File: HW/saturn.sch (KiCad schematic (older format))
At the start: 0 parts

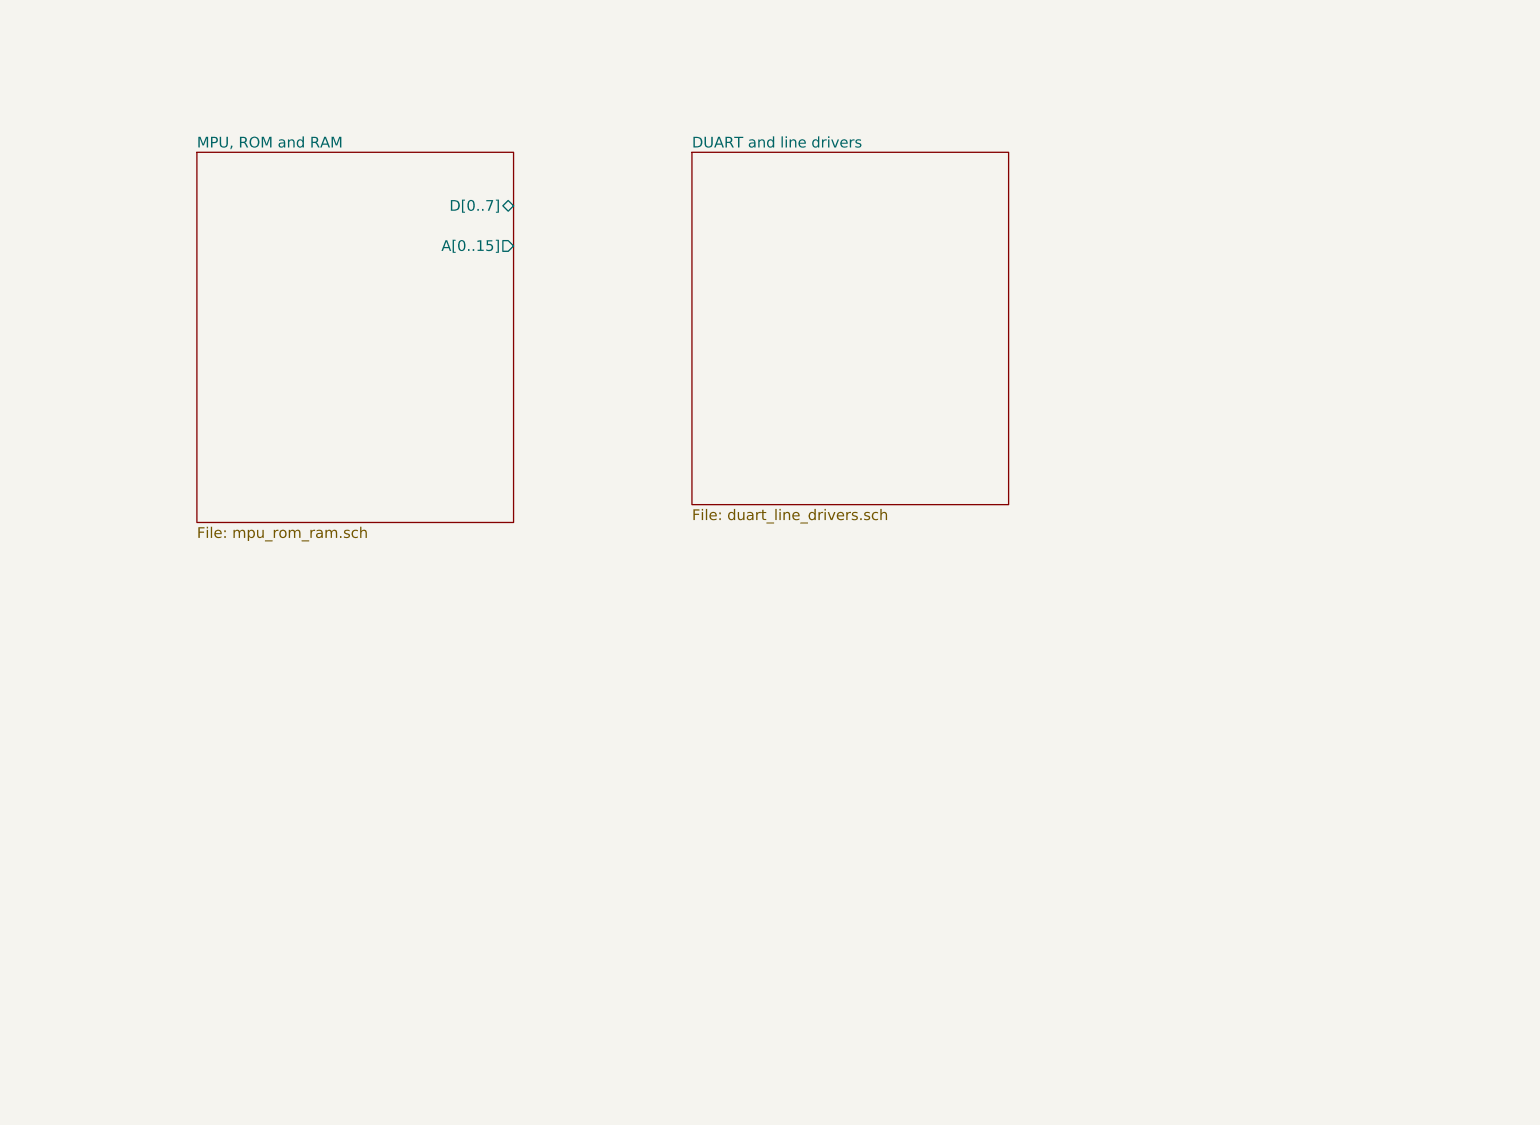
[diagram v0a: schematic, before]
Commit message: Added ram, vias, rtc and ide connector. Managed to delete Pluto's CPLD schemas.
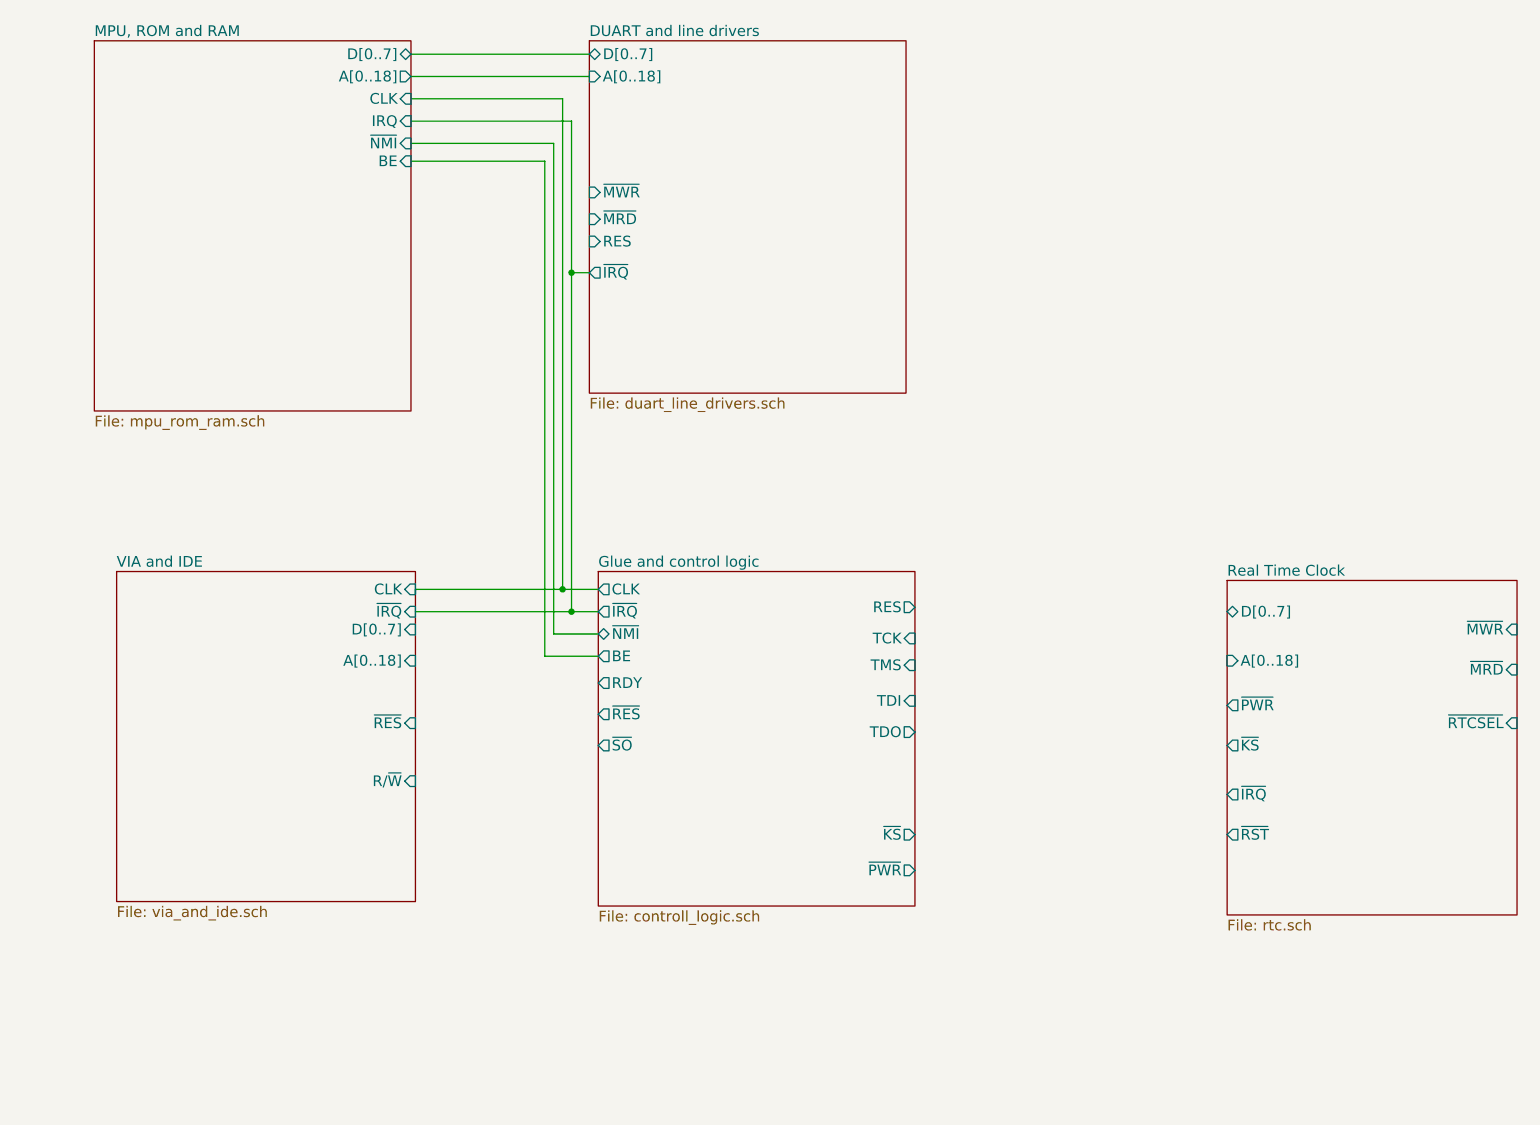
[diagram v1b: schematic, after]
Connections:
- wire segments 0 -> 16
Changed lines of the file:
@@
 EESchema Schematic File Version 2
+LIBS:saturn-rescue
 LIBS:power
 LIBS:device
@@
 LIBS:contrib
 LIBS:valves
+LIBS:saturn
+LIBS:65xx
 LIBS:pluto
-LIBS:65xx
+LIBS:Oscillators
+LIBS:switches
 LIBS:saturn-cache
 EELAYER 25 0
@@
 $Descr A4 11693 8268
 encoding utf-8
-Sheet 1 3
+Sheet 1 6
 Title "Saturn SBC"
 Date "2017-06-28"
@@
 $EndDescr
 $Sheet
-S 1800 1625 1775 2075
+S 1225 1000 1775 2075
 U 5952FC78
 F0 "MPU, ROM and RAM" 60
 F1 "mpu_rom_ram.sch" 60
-F2 "D[0..7]" B R 3575 1925 60
-F3 "A[0..15]" O R 3575 2150 60
+F2 "D[0..7]" B R 3000 1075 60
+F3 "A[0..18]" O R 3000 1200 60
+F4 "CLK" I R 3000 1325 60
+F5 "IRQ" I R 3000 1450 60
+F6 "~NMI" I R 3000 1575 60
+F7 "BE" I R 3000 1675 60
 $EndSheet
 $Sheet
-S 4575 1625 1775 1975
+S 4000 1000 1775 1975
 U 5952FC81
 F0 "DUART and line drivers" 60
 F1 "duart_line_drivers.sch" 60
+F2 "D[0..7]" B L 4000 1075 60
+F3 "~MWR" I L 4000 1850 60
+F4 "~MRD" I L 4000 2000 60
+F5 "RES" I L 4000 2125 60
+F6 "~IRQ" O L 4000 2300 60
+F7 "A[0..18]" I L 4000 1200 60
+$EndSheet
+Wire Wire Line
+	3000 1075 4000 1075
+Wire Wire Line
+	3000 1200 4000 1200
+$Sheet
+S 1350 3975 1675 1850
+U 5A3B21BC
+F0 "VIA and IDE" 60
+F1 "via_and_ide.sch" 60
+F2 "D[0..7]" I R 3025 4300 60
+F3 "A[0..18]" I R 3025 4475 60
+F4 "CLK" I R 3025 4075 60
+F5 "~RES" I R 3025 4825 60
+F6 "~IRQ" I R 3025 4200 60
+F7 "R/~W" I R 3025 5150 60
+$EndSheet
+$Sheet
+S 4050 3975 1775 1875
+U 5A3B356D
+F0 "Glue and control logic" 60
+F1 "controll_logic.sch" 60
+F2 "CLK" O L 4050 4075 60
+F3 "~IRQ" O L 4050 4200 60
+F4 "~NMI" B L 4050 4325 60
+F5 "BE" O L 4050 4450 60
+F6 "RDY" O L 4050 4600 60
+F7 "~PWR" O R 5825 5650 60
+F8 "~RES" O L 4050 4775 60
+F9 "~SO" O L 4050 4950 60
+F10 "RES" O R 5825 4175 60
+F11 "TCK" I R 5825 4350 60
+F12 "TMS" I R 5825 4500 60
+F13 "TDI" I R 5825 4700 60
+F14 "TDO" O R 5825 4875 60
+F15 "~KS" O R 5825 5450 60
+$EndSheet
+Wire Wire Line
+	3000 1450 3900 1450
+Wire Wire Line
+	3900 1450 3900 4200
+Wire Wire Line
+	3900 2300 4000 2300
+Wire Wire Line
+	3025 4200 4050 4200
+Connection ~ 3900 2300
+Wire Wire Line
+	3000 1325 3850 1325
+Wire Wire Line
+	3850 1325 3850 4075
+Wire Wire Line
+	3025 4075 4050 4075
+Wire Wire Line
+	3000 1575 3800 1575
+Wire Wire Line
+	3800 1575 3800 4325
+Wire Wire Line
+	3800 4325 4050 4325
+Wire Wire Line
+	3000 1675 3750 1675
+Wire Wire Line
+	3750 1675 3750 4450
+Wire Wire Line
+	3750 4450 4050 4450
+Wire Wire Line
+	3025 4100 3025 4075
+Connection ~ 3850 4075
+Connection ~ 3900 4200
+$Sheet
+S 7575 4025 1625 1875
+U 5A3D7428
+F0 "Real Time Clock" 60
+F1 "rtc.sch" 60
+F2 "D[0..7]" B L 7575 4200 60
+F3 "A[0..18]" I L 7575 4475 60
+F4 "~PWR" O L 7575 4725 60
+F5 "~KS" O L 7575 4950 60
+F6 "~IRQ" O L 7575 5225 60
+F7 "~RST" O L 7575 5450 60
+F8 "~MWR" I R 9200 4300 60
+F9 "~MRD" I R 9200 4525 60
+F10 "~RTCSEL" I R 9200 4825 60
 $EndSheet
 $EndSCHEMATC

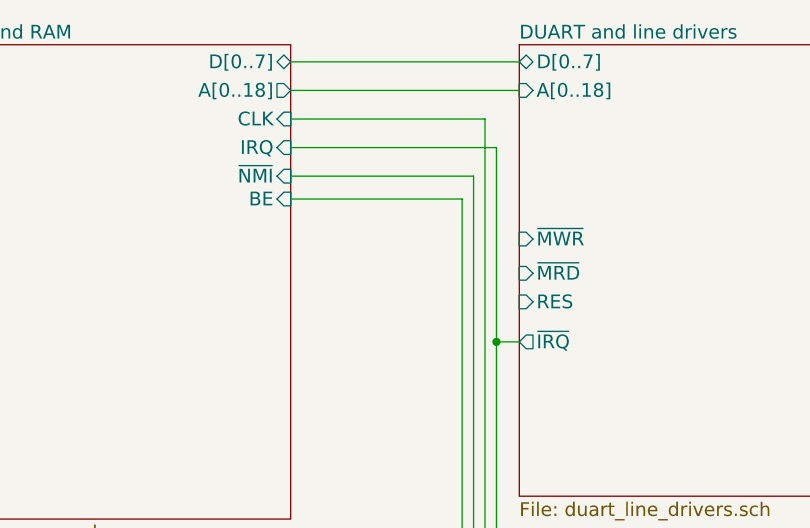
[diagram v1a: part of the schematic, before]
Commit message: Address, databus and control signals added to RAM and ROM
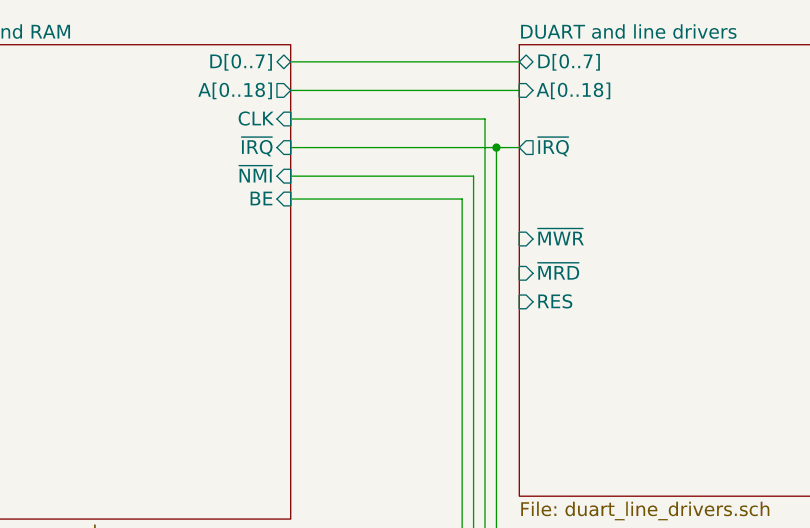
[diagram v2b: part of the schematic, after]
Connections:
- wire segments 16 -> 15
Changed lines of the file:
@@
 Sheet 1 6
 Title "Saturn SBC"
-Date "2017-06-28"
-Rev "1.0"
+Date "2017-12-23"
+Rev "0.1"
 Comp "Linux Grotto"
-Comment1 ""
-Comment2 ""
-Comment3 ""
-Comment4 ""
+Comment1 "Control logic is implemented using an ispMACH4A5"
+Comment2 "IDE interface realised with two VIA 65C22"
+Comment3 "Serial Communication with a 28L92 and MAX238"
+Comment4 "Real Time clock, a DS1511Y"
 $EndDescr
 $Sheet
@@
 F3 "A[0..18]" O R 3000 1200 60
 F4 "CLK" I R 3000 1325 60
-F5 "IRQ" I R 3000 1450 60
-F6 "~NMI" I R 3000 1575 60
-F7 "BE" I R 3000 1675 60
+F5 "~NMI" I R 3000 1575 60
+F6 "BE" I R 3000 1675 60
+F7 "~IRQ" I R 3000 1450 60
 $EndSheet
 $Sheet
@@
 F4 "~MRD" I L 4000 2000 60
 F5 "RES" I L 4000 2125 60
-F6 "~IRQ" O L 4000 2300 60
+F6 "~IRQ" O L 4000 1450 60
 F7 "A[0..18]" I L 4000 1200 60
 $EndSheet
@@
 $EndSheet
 Wire Wire Line
-	3000 1450 3900 1450
+	3000 1450 4000 1450
 Wire Wire Line
 	3900 1450 3900 4200
 Wire Wire Line
-	3900 2300 4000 2300
-Wire Wire Line
 	3025 4200 4050 4200
-Connection ~ 3900 2300
 Wire Wire Line
 	3000 1325 3850 1325
@@
 F10 "~RTCSEL" I R 9200 4825 60
 $EndSheet
+Connection ~ 3900 1450
 $EndSCHEMATC

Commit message: Finished RAM/ROM/CPU control signals.
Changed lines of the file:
@@
 F6 "BE" I R 3000 1675 60
 F7 "~IRQ" I R 3000 1450 60
+F8 "~MRD" I L 1225 2075 60
+F9 "~MWR" I L 1225 1675 60
+F10 "~RAM0" I L 1225 1800 60
+F11 "~RAM1" I L 1225 1925 60
+F12 "~ROM" I L 1225 2200 60
+F13 "R/~W" O L 1225 2325 60
+F14 "VDA" O L 1225 2425 60
+F15 "VPA" O L 1225 2550 60
+F16 "~RES" I L 1225 2700 60
+F17 "/ABT" I L 1225 1550 60
+F18 "RDY" I L 1225 1425 60
 $EndSheet
 $Sheet

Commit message: Simulation of address decoding.
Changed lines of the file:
@@
 F1 "mpu_rom_ram.sch" 60
 F2 "D[0..7]" B R 3000 1075 60
-F3 "A[0..18]" O R 3000 1200 60
+F3 "A[0..19]" O R 3000 1200 60
 F4 "CLK" I R 3000 1325 60
 F5 "~NMI" I R 3000 1575 60
@@
 F17 "/ABT" I L 1225 1550 60
 F18 "RDY" I L 1225 1425 60
+F19 "~ABT" I R 3000 1850 60
 $EndSheet
 $Sheet
@@
 F5 "RES" I L 4000 2125 60
 F6 "~IRQ" O L 4000 1450 60
-F7 "A[0..18]" I L 4000 1200 60
+F7 "A[0..19]" I L 4000 1200 60
+F8 "~DUARTSEL" I L 4000 1650 60
 $EndSheet
 Wire Wire Line
@@
 F1 "via_and_ide.sch" 60
 F2 "D[0..7]" I R 3025 4300 60
-F3 "A[0..18]" I R 3025 4475 60
+F3 "A[0..19]" I R 3025 4475 60
 F4 "CLK" I R 3025 4075 60
 F5 "~RES" I R 3025 4825 60
@@
 F1 "rtc.sch" 60
 F2 "D[0..7]" B L 7575 4200 60
-F3 "A[0..18]" I L 7575 4475 60
+F3 "A[0..19]" I L 7575 4475 60
 F4 "~PWR" O L 7575 4725 60
 F5 "~KS" O L 7575 4950 60

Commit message: ABEL code passes compilation, no tests though. Small changes to schema
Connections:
- net labels added: A[0..18], D[0..7]
- wire segments 15 -> 74

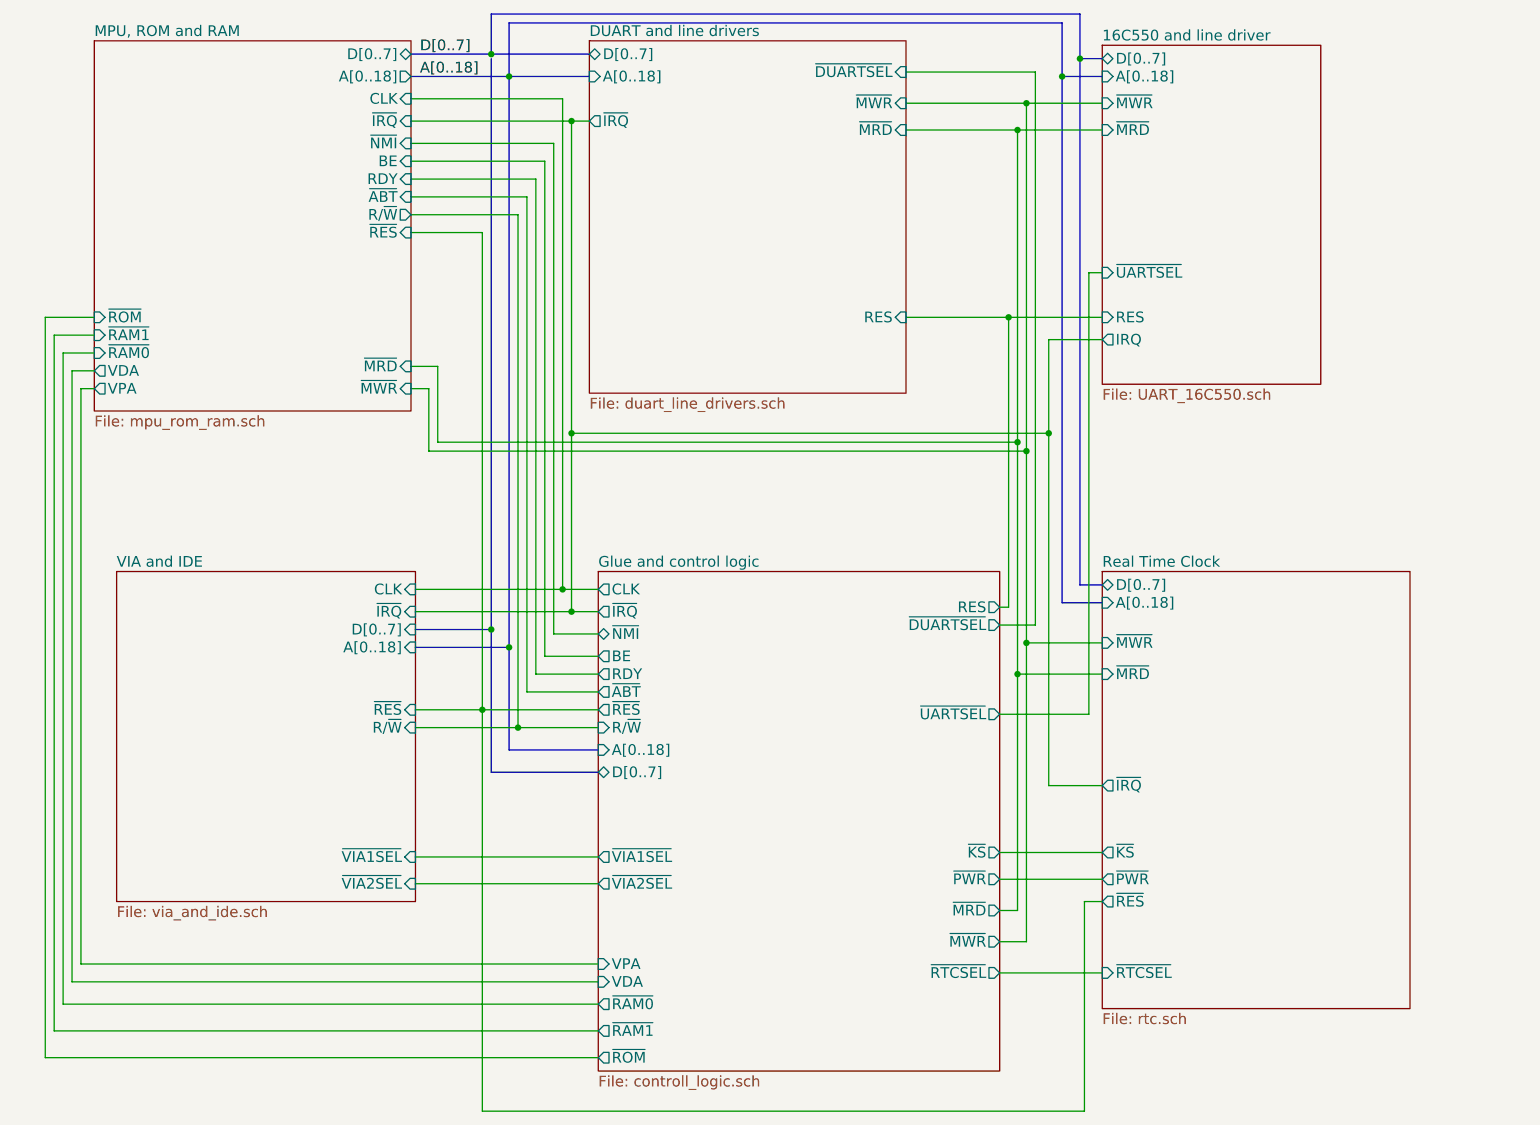
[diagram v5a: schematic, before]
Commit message: Removed two ram chips, down to 1 MiB.
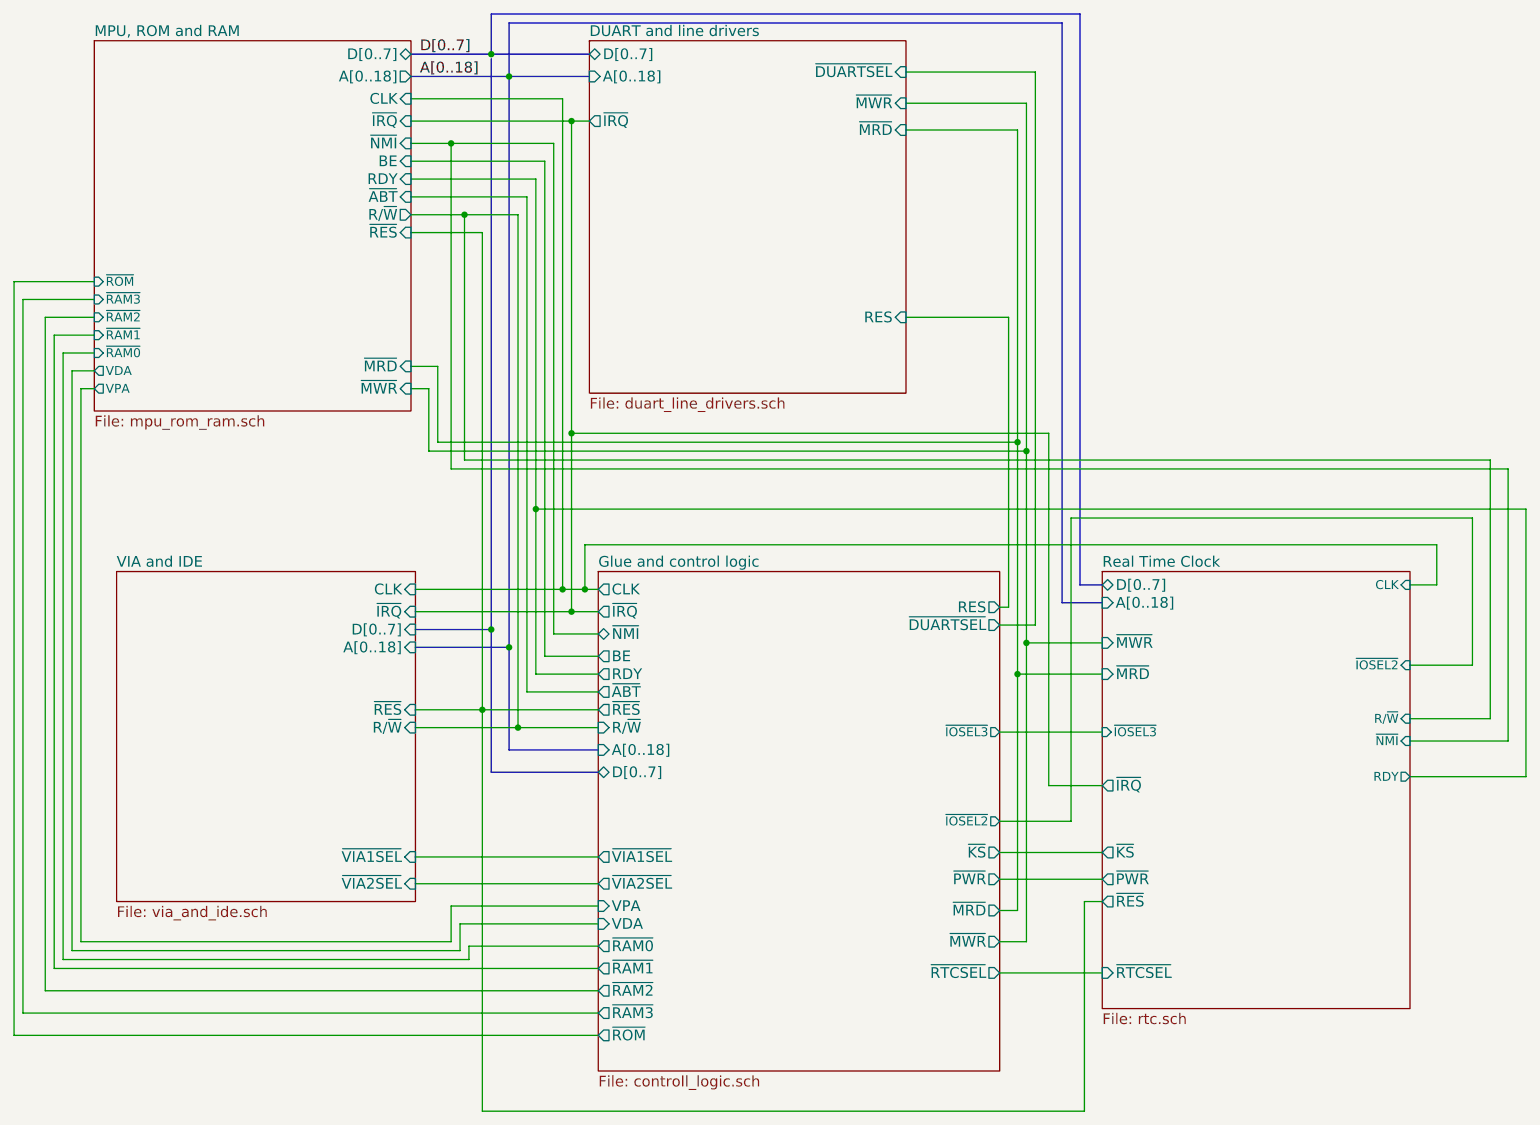
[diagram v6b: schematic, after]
